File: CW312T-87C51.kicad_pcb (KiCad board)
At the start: 2 copper layers, 58.7 x 53.7 mm, 43 parts, among them J1 1x3 straight header pins, J10 2Pin_Header_2.54, J11 1x3 straight header pins, J2 1x3 straight header pins, J3 1x3 straight header pins, J4 1x3 straight header pins, J5 1x3 straight header pins, J6 1x3 straight header pins, J7 1x3 straight header pins, J8 68000-220HLF, J9 68000-220HLF, P1 PCIEx4 EDGE CONNECTOR, U1 87C51, U2 ATMEGA325PA-AU, Y1 ABMM2-7.3728MHZ-E2-T

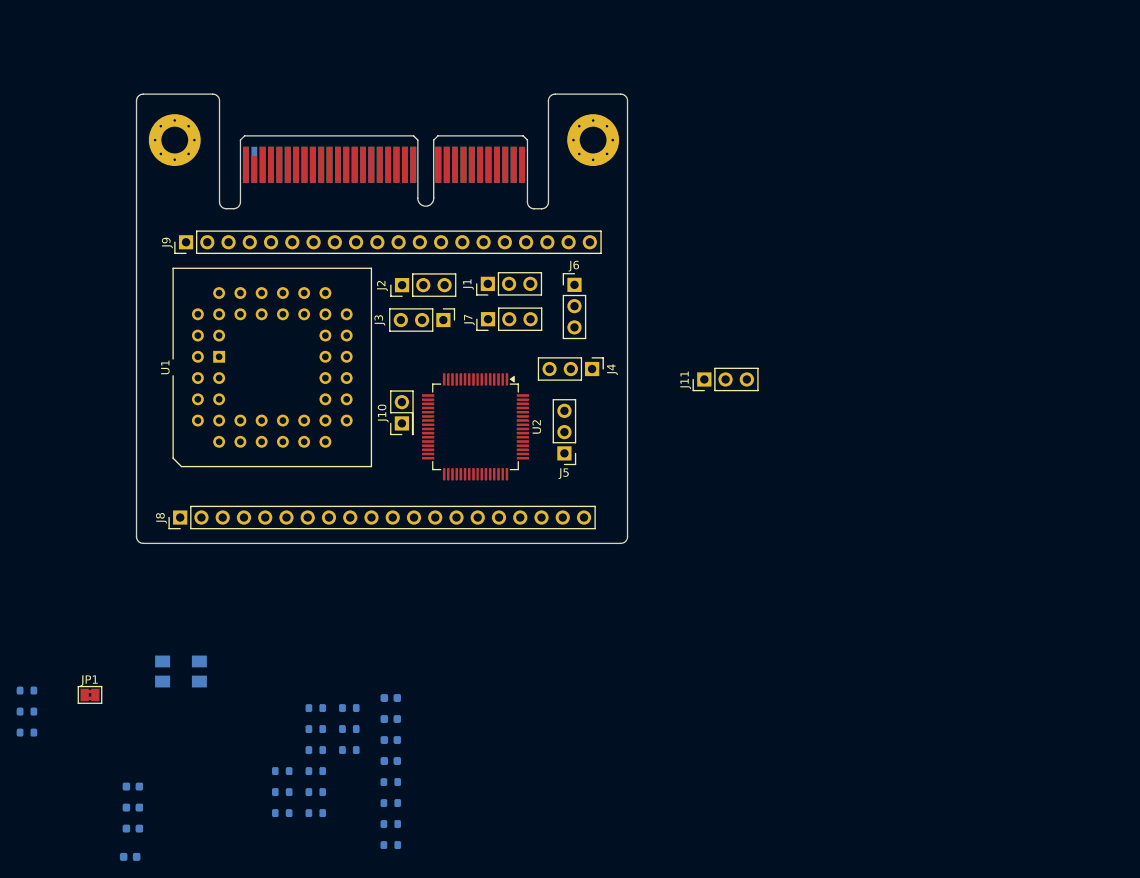
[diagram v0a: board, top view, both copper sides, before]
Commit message: updated schematic after library re-organization
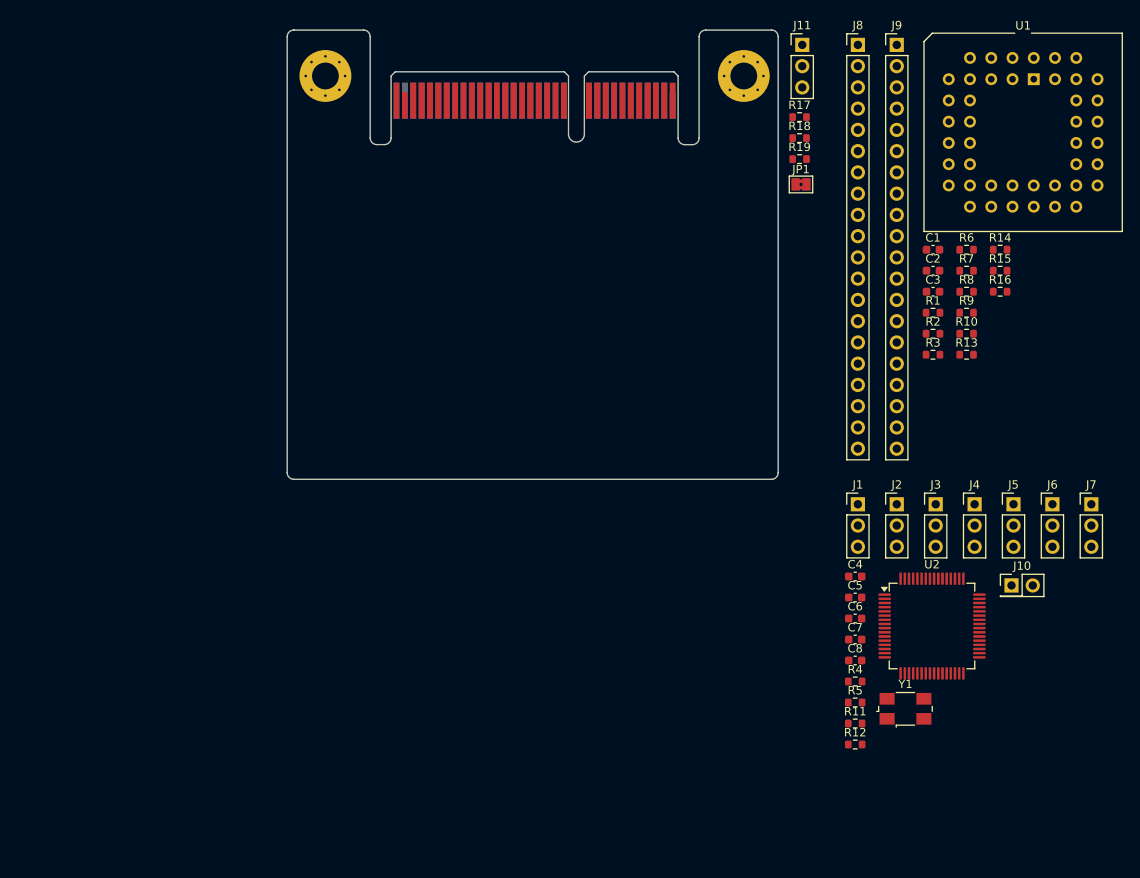
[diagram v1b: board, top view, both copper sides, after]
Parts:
- C1, C2, C3, C4, C5, C6, C7, C8, R1, R10, R11, R12, R13, R14, R15, R16, R17, R18, R19, R2, R3, R4, R5, R6, R7, R8, R9, Y1: moved to F.Cu
- moved C1 115.2 mm to (165.9, 81.4), turned to 0 degrees
- moved C2 115.2 mm to (165.9, 83.9), turned to 0 degrees
- moved C3 115.2 mm to (165.9, 86.4), turned to 0 degrees
- moved R17 115.0 mm to (149.9, 65.5), turned to 0 degrees
- moved R18 115.0 mm to (149.9, 68.0), turned to 0 degrees
- moved R19 115.0 mm to (149.9, 70.5), turned to 0 degrees
- moved JP1 104.6 mm to (150.1, 73.6)
- moved U1 102.9 mm to (177.9, 61.0), turned to 0 degrees
- moved J8 98.7 mm to (156.9, 56.9), turned to 0 degrees
- moved R1 95.1 mm to (165.9, 88.9), turned to 0 degrees
- moved R14 95.1 mm to (173.9, 81.4), turned to 0 degrees
- moved R15 95.1 mm to (173.9, 83.9), turned to 0 degrees
- moved R2 95.1 mm to (165.9, 91.4), turned to 0 degrees
- moved R10 95.1 mm to (169.9, 91.4), turned to 0 degrees
- moved R13 95.1 mm to (169.9, 93.9), turned to 0 degrees
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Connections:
- J7 pad 1: GND -> unconnected-(J7-Pad1)
- J7 pad 3: unconnected-(J7-Pad3) -> GND
